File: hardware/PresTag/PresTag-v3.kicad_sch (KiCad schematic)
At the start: 20 parts, among them J201 CONN_02X04, J301 Conn_01x01, J302 Conn_01x01, J303 Conn_01x01, J304 Conn_01x01, J401 CONN_01X02, Q501 Q_NPN_BEC, U1 at25ex321D-UUN, U501 RV-3028-C7

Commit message: update PresTag components
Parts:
- C101: DISTPN GRM033R60J105MEA2D -> 490-7229-1-ND; MPN 490-7229-1-ND -> GRM033R60J105MEA2D
- U2: value (none) -> LPS27HHWTR; DISTPN (none) -> 497-LPS27HHWCT-ND; MFN (none) -> STMicroelectronics; MPN (none) -> LPS27HHWTR
- U302: value (none) -> stm32l431kc; footprint (none) -> Package_DFN_QFN:QFN-32-1EP_5x5mm_P0.5mm_EP3.45x3.45mm; DISTPN 497-16578-ND -> 497-17958-ND; MPN STM32L432KCU6 -> STM32L431KCU6
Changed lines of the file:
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@@
       (effects (font (size 1.524 1.524)) (justify right))
     )
-    (property "Value" "" (id 1) (at 128.27 93.98 0)
+    (property "Value" "stm32l431kc" (id 1) (at 128.27 93.98 0)
       (effects (font (size 1.524 1.524)) (justify right))
     )
-    (property "Footprint" "" (id 2) (at 87.63 76.2 0)
+    (property "Footprint" "Package_DFN_QFN:QFN-32-1EP_5x5mm_P0.5mm_EP3.45x3.45mm" (id 2) (at 87.63 76.2 0)
       (effects (font (size 1.524 1.524)) hide)
     )
@@
       (effects (font (size 1.524 1.524)) hide)
     )
-    (property "DISTPN" "497-16578-ND" (id 5) (at 87.63 76.2 0)
-      (effects (font (size 1.524 1.524)) hide)
-    )
-    (property "MPN" "STM32L432KCU6" (id 6) (at 0 152.4 0)
+    (property "DISTPN" "497-17958-ND" (id 5) (at 87.63 76.2 0)
+      (effects (font (size 1.524 1.524)) hide)
+    )
+    (property "MPN" "STM32L431KCU6" (id 6) (at 0 152.4 0)
       (effects (font (size 1.27 1.27)) hide)
     )
@@
       (effects (font (size 1.524 1.524)))
     )
-    (property "Value" "" (id 1) (at 80.645 136.3726 0)
+    (property "Value" "LPS27HHWTR" (id 1) (at 80.645 136.3726 0)
       (effects (font (size 1.524 1.524)))
     )
@@
     (property "Datasheet" "" (id 3) (at 59.69 140.97 0)
       (effects (font (size 1.524 1.524)))
+    )
+    (property "DISTPN" "497-LPS27HHWCT-ND" (id 4) (at 59.69 140.97 0)
+      (effects (font (size 1.27 1.27)) hide)
+    )
+    (property "MFN" "STMicroelectronics" (id 5) (at 59.69 140.97 0)
+      (effects (font (size 1.27 1.27)) hide)
+    )
+    (property "MPN" "LPS27HHWTR" (id 6) (at 59.69 140.97 0)
+      (effects (font (size 1.27 1.27)) hide)
     )
     (pin "1")
@@
       (effects (font (size 1.524 1.524)) hide)
     )
-    (property "MPN" "490-7229-1-ND" (id 6) (at 189.23 100.33 0)
-      (effects (font (size 1.524 1.524)) hide)
-    )
-    (property "DISTPN" "GRM033R60J105MEA2D" (id 7) (at 120.65 198.12 0)
+    (property "MPN" "GRM033R60J105MEA2D" (id 6) (at 189.23 100.33 0)
+      (effects (font (size 1.524 1.524)) hide)
+    )
+    (property "DISTPN" "490-7229-1-ND" (id 7) (at 120.65 198.12 0)
       (effects (font (size 1.27 1.27)) hide)
     )
@@
       (effects (font (size 1.27 1.27)) hide)
     )
-    (property "Value" "" (id 1) (at 104.14 44.45 0))
+    (property "Value" "PWR_FLAG" (id 1) (at 104.14 44.45 0))
     (property "Footprint" "" (id 2) (at 104.14 49.53 0)
       (effects (font (size 1.27 1.27)) hide)

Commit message: update prestag for manufacturing
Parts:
- U302: DISTPN 497-17958-ND -> 497-STM32L412K8U6-ND; MPN STM32L431KCU6 -> STM32L412K8U6
- U501: DISTPN 2195-RV-3028-C732.768KHZ1PPM-TA-QACT-ND -> 2195-RV-3028-C732.768KHZ1PPM-TA-QCCT-ND; MPN RV-3028-C7 32.768KHZ 1PPM-TA-QA -> RV-3028-C7 32.768KHZ 1PPM-TA-QC
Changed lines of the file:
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@@
       (effects (font (size 1.524 1.524)) hide)
     )
-    (property "DISTPN" "497-17958-ND" (id 5) (at 87.63 76.2 0)
-      (effects (font (size 1.524 1.524)) hide)
-    )
-    (property "MPN" "STM32L431KCU6" (id 6) (at 0 152.4 0)
+    (property "DISTPN" "497-STM32L412K8U6-ND" (id 5) (at 87.63 76.2 0)
+      (effects (font (size 1.524 1.524)) hide)
+    )
+    (property "MPN" "STM32L412K8U6" (id 6) (at 0 152.4 0)
       (effects (font (size 1.27 1.27)) hide)
     )
@@
       (effects (font (size 1.524 1.524)) hide)
     )
-    (property "DISTPN" "2195-RV-3028-C732.768KHZ1PPM-TA-QACT-ND" (id 4) (at 26.67 335.28 0)
+    (property "DISTPN" "2195-RV-3028-C732.768KHZ1PPM-TA-QCCT-ND" (id 4) (at 26.67 335.28 0)
       (effects (font (size 1.27 1.27)) hide)
     )
@@
       (effects (font (size 1.27 1.27)) hide)
     )
-    (property "MPN" "RV-3028-C7 32.768KHZ 1PPM-TA-QA" (id 6) (at 26.67 335.28 0)
-      (effects (font (size 1.27 1.27)) hide)
-    )
+    (property "MPN" "RV-3028-C7 32.768KHZ 1PPM-TA-QC" (id 6) (at 26.67 335.28 0)
+      (effects (font (size 1.27 1.27)) hide)
+    )

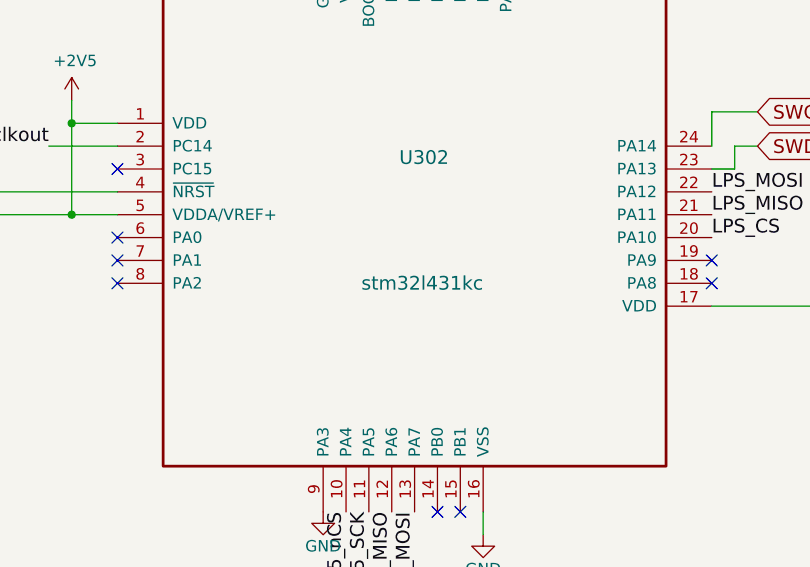
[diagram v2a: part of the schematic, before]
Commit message: update Prestag
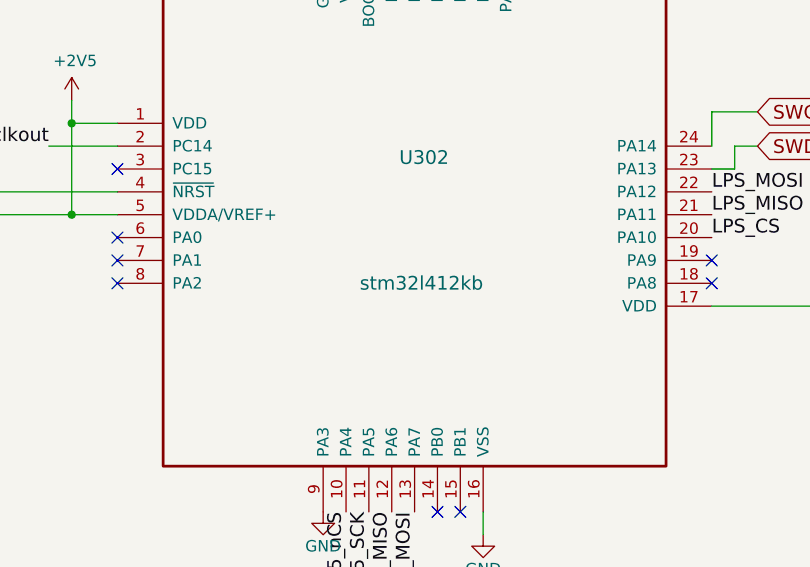
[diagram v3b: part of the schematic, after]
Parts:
- U302: value stm32l431kc -> stm32l412kb
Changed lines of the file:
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@@
       (effects (font (size 1.524 1.524)) (justify right))
     )
-    (property "Value" "stm32l431kc" (id 1) (at 128.27 93.98 0)
+    (property "Value" "stm32l412kb" (id 1) (at 128.27 93.98 0)
       (effects (font (size 1.524 1.524)) (justify right))
     )
@@
     )
     (path "/00000000-0000-0000-0000-000058a7531d"
-      (reference "U302") (unit 1) (value "stm32l431kc") (footprint "Package_DFN_QFN:QFN-32-1EP_5x5mm_P0.5mm_EP3.45x3.45mm")
+      (reference "U302") (unit 1) (value "stm32l412kb") (footprint "Package_DFN_QFN:QFN-32-1EP_5x5mm_P0.5mm_EP3.45x3.45mm")
     )
     (path "/00000000-0000-0000-0000-00005ef60ddb"

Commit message: revise prestag
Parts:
- U2: footprint QFN_HHWTR_STM -> lib_fp:LPS27HHWTR
- U302: value stm32l412kb -> stm32l431kc; DISTPN 497-STM32L412K8U6-ND -> 511-STM32L431KCU6; MPN STM32L412K8U6 -> STM32L431KCU6
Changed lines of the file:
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@@
       (effects (font (size 1.524 1.524)) (justify right))
     )
-    (property "Value" "stm32l412kb" (id 1) (at 128.27 93.98 0)
+    (property "Value" "stm32l431kc" (id 1) (at 128.27 93.98 0)
       (effects (font (size 1.524 1.524)) (justify right))
     )
@@
       (effects (font (size 1.524 1.524)) hide)
     )
-    (property "DISTPN" "497-STM32L412K8U6-ND" (id 5) (at 87.63 76.2 0)
-      (effects (font (size 1.524 1.524)) hide)
-    )
-    (property "MPN" "STM32L412K8U6" (id 6) (at 0 152.4 0)
+    (property "DISTPN" "511-STM32L431KCU6" (id 5) (at 87.63 76.2 0)
+      (effects (font (size 1.524 1.524)) hide)
+    )
+    (property "MPN" "STM32L431KCU6" (id 6) (at 0 152.4 0)
       (effects (font (size 1.27 1.27)) hide)
     )
@@
       (effects (font (size 1.524 1.524)))
     )
-    (property "Footprint" "QFN_HHWTR_STM" (id 2) (at 80.645 132.715 0)
+    (property "Footprint" "lib_fp:LPS27HHWTR" (id 2) (at 80.645 132.715 0)
       (effects (font (size 1.524 1.524)) hide)
     )
@@
     )
     (path "/00000000-0000-0000-0000-000060c8320f"
-      (reference "U2") (unit 1) (value "LPS27HHWTR") (footprint "QFN_HHWTR_STM")
+      (reference "U2") (unit 1) (value "LPS27HHWTR") (footprint "lib_fp:LPS27HHWTR")
     )
     (path "/00000000-0000-0000-0000-000058a7531d"
-      (reference "U302") (unit 1) (value "stm32l412kb") (footprint "Package_DFN_QFN:QFN-32-1EP_5x5mm_P0.5mm_EP3.45x3.45mm")
+      (reference "U302") (unit 1) (value "stm32l431kc") (footprint "Package_DFN_QFN:QFN-32-1EP_5x5mm_P0.5mm_EP3.45x3.45mm")
     )
     (path "/00000000-0000-0000-0000-00005ef60ddb"
